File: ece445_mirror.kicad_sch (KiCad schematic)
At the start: 47 parts, among them J1 Conn_01x04, J2 Conn_ARM_SWD_TagConnect_TC2030, J3 Conn_01x06, J4 USB_C_Receptacle_USB2.0_14P, SW1 SW_Push, SW2 SW_Push, U1 STM32F405RGT7, U2 STM32F401RBTx, U3 USBLC6-2SC6, U4 AP2112K-3.3, Y1 25MHz

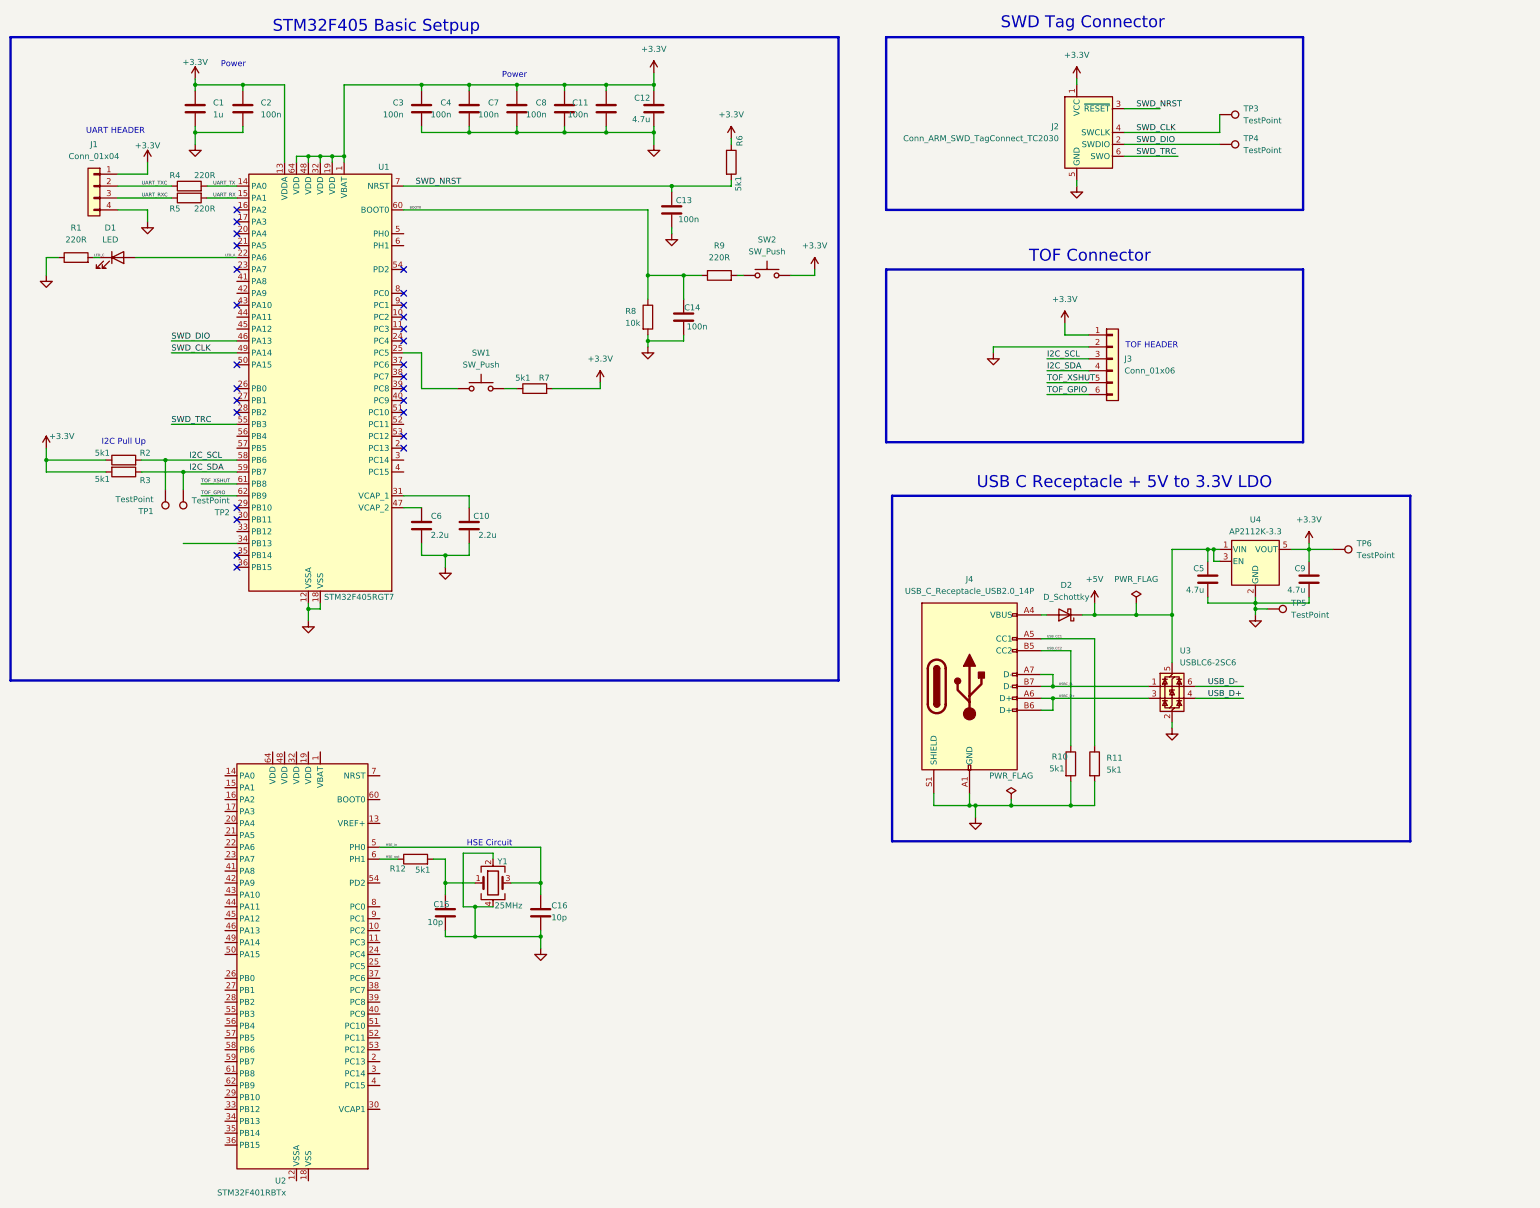
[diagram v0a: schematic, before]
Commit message: schematic completed; changed chip; added HSE, vref+
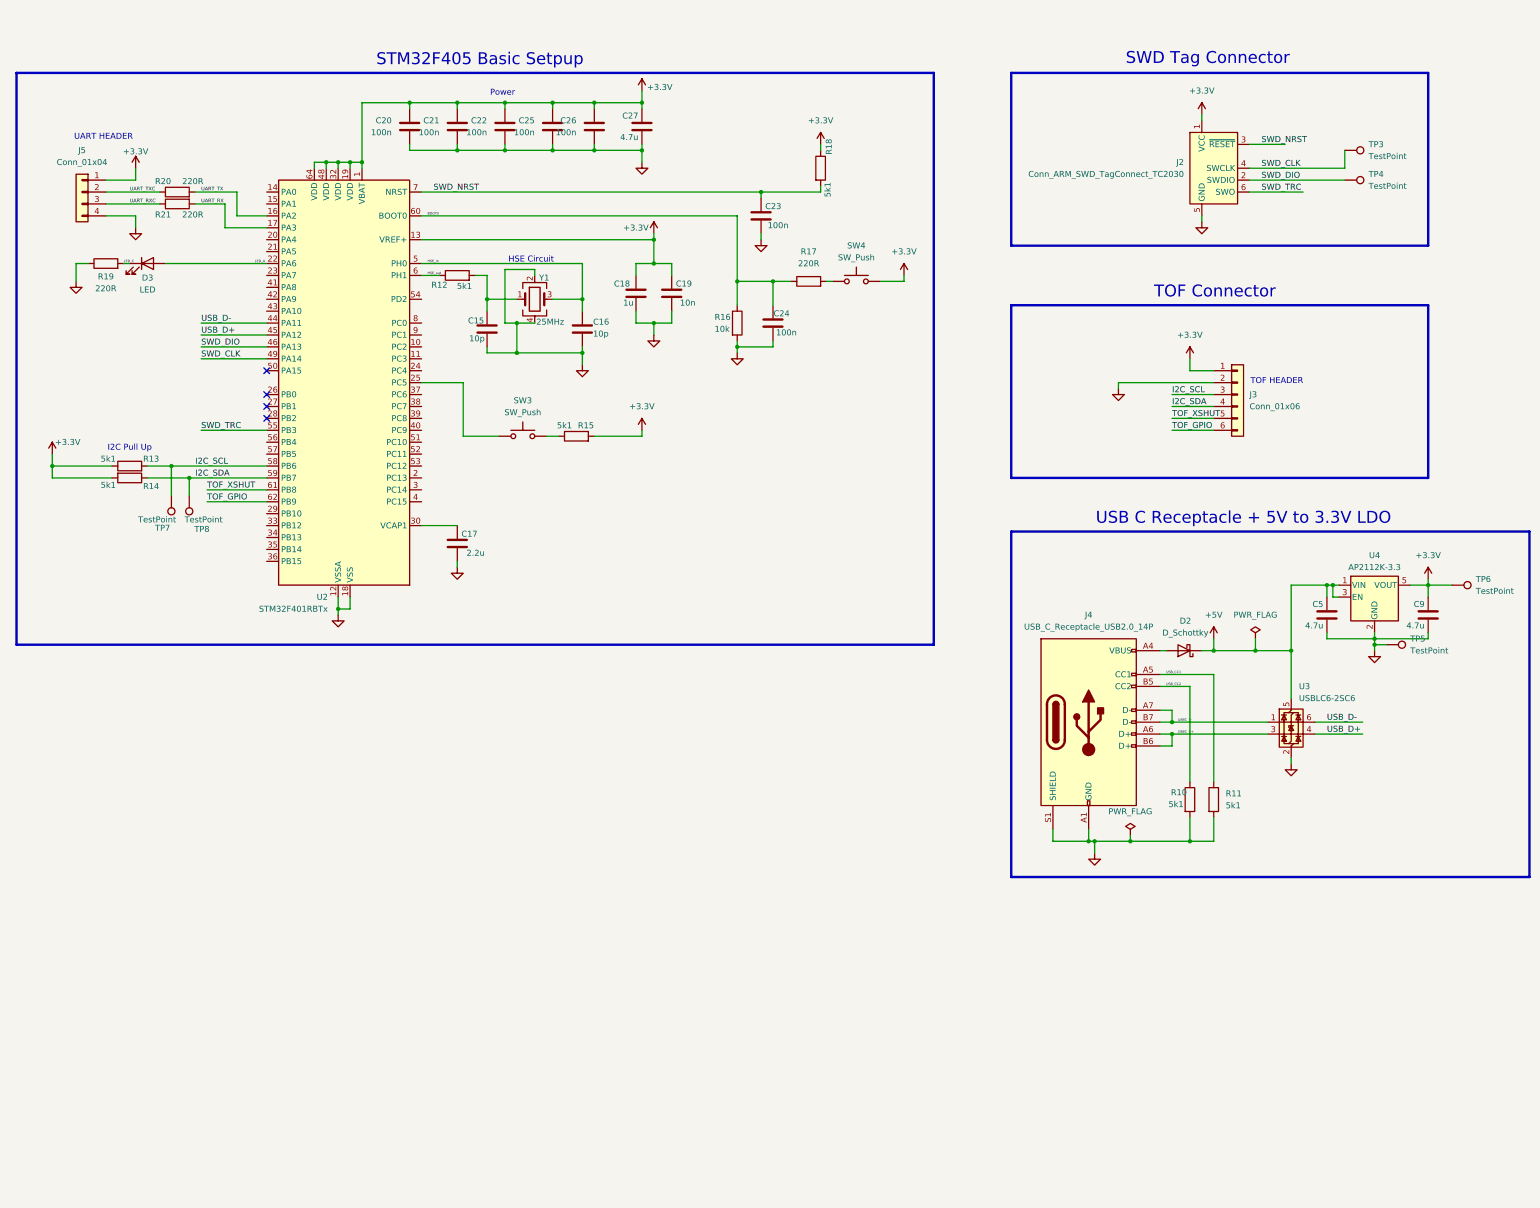
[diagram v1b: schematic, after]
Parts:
- removed C1: 1u, Capacitor_SMD:C_0402_1005Metric, symbol Device:C
- removed C10, C6: 2.2u, Capacitor_SMD:C_0402_1005Metric, symbol Device:C
- removed C11, C13, C14, C2, C3, C4, C7, C8: 100n, Capacitor_SMD:C_0402_1005Metric, symbol Device:C
- removed C12: 4.7u, Capacitor_SMD:C_0805_2012Metric, symbol Device:C
- removed D1: LED, LED_SMD:LED_CSP_Samsung_LH181B_2.36x2.36mm, symbol Device:LED
- removed J1: Conn_01x04, Connector_Molex:Molex_PicoBlade_53261-0471_1x04-1MP_P1.25mm_Horizontal, symbol Connector_Generic:Conn_01x04
- removed R1, R4, R5, R9: 220R, Resistor_SMD:R_0402_1005Metric, symbol Device:R
- removed R2, R3, R6, R7: 5k1, Resistor_SMD:R_0402_1005Metric, symbol Device:R
- removed R8: 10k, Resistor_SMD:R_0402_1005Metric, symbol Device:R
- removed SW1, SW2: SW_Push, Button_Switch_SMD:SW_SPST_CK_RS282G05A3, symbol Switch:SW_Push
- removed TP1, TP2: TestPoint, TestPoint:TestPoint_Pad_2.0x2.0mm, symbol Connector:TestPoint
- removed U1: STM32F405RGT7, Package_QFP:LQFP-64_10x10mm_P0.5mm, symbol MCU_ST_STM32F4:STM32F405RGTx
- added C17: 2.2u, Capacitor_SMD:C_0402_1005Metric, symbol Device:C
- added C18: 1u, Capacitor_SMD:C_0402_1005Metric, symbol Device:C
- added C19: 10n, Capacitor_SMD:C_0402_1005Metric, symbol Device:C
- added C20, C21, C22, C23, C24, C25, C26: 100n, Capacitor_SMD:C_0402_1005Metric, symbol Device:C
- added C27: 4.7u, Capacitor_SMD:C_0805_2012Metric, symbol Device:C
- added D3: LED, LED_SMD:LED_CSP_Samsung_LH181B_2.36x2.36mm, symbol Device:LED
- added J5: Conn_01x04, Connector_Molex:Molex_PicoBlade_53261-0471_1x04-1MP_P1.25mm_Horizontal, symbol Connector_Generic:Conn_01x04
- added R13, R14, R15, R18: 5k1, Resistor_SMD:R_0402_1005Metric, symbol Device:R
- added R16: 10k, Resistor_SMD:R_0402_1005Metric, symbol Device:R
- added R17, R19, R20, R21: 220R, Resistor_SMD:R_0402_1005Metric, symbol Device:R
- added SW3, SW4: SW_Push, Button_Switch_SMD:SW_SPST_CK_RS282G05A3, symbol Switch:SW_Push
- added TP7, TP8: TestPoint, TestPoint:TestPoint_Pad_2.0x2.0mm, symbol Connector:TestPoint
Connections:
- net +3.3V: now also U2.1 (VBAT), U2.13 (VREF+), U2.19 (VDD), U2.32 (VDD), U2.48 (VDD), U2.64 (VDD), C18.1, C19.1, C20.1, C21.1, C22.1, C25.1, C26.1, C27.1, J5.1 (Pin_1), R13.1, R14.2, R15.2, R18.1, SW4.2
- net BOOT0: now also U2.60 (BOOT0), C24.1, R16.1, R17.1
- net GND: now also U2.12 (VSSA), U2.18 (VSS), U2.31 (VSS), U2.47 (VSS), U2.63 (VSS), C17.2, C18.2, C19.2, C20.2, C21.2, C22.2, C23.2, C24.2, C25.2, C26.2, C27.2, J5.4 (Pin_4), R16.2, R19.1
- net I2C_SCL: now also U2.58 (PB6), R13.2, TP7.1
- net I2C_SDA: now also U2.59 (PB7), R14.1, TP8.1
- net LED_A: now also U2.22 (PA6), D3.2 (A)
- net LED_C: now also D3.1 (K), R19.2
- net SWD_CLK: now also U2.49 (PA14)
- net SWD_DIO: now also U2.46 (PA13)
- net SWD_NRST: now also U2.7 (NRST), C23.1, R18.2
- net SWD_TRC: now also U2.55 (PB3)
- net TOF_GPIO: now also U2.62 (PB9)
- net TOF_XSHUT: now also U2.61 (PB8)
- net UART_RX: now also U2.17 (PA3), R21.2
- net UART_RXC: now also J5.3 (Pin_3), R21.1
- net UART_TX: now also U2.16 (PA2), R20.2
- net UART_TXC: now also J5.2 (Pin_2), R20.1
- net USB_D+: now also U2.45 (PA12)
- net USB_D-: now also U2.44 (PA11)
- net at U2.25 (PC5): now also SW3.1
- net at U2.30 (VCAP1): now also C17.1
- new net: R17.2, SW4.1
- new net: R15.1, SW3.2
- no-connect marks 27 -> 4
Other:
- moved on the sheet: C15, C16, C5, C9, D2, J2, J3, J4, R10, R11, R12, TP3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

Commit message: footprints!
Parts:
- removed D3: LED, LED_SMD:LED_CSP_Samsung_LH181B_2.36x2.36mm, symbol Device:LED
- removed J2: Conn_ARM_SWD_TagConnect_TC2030, Connector:Tag-Connect_TC2030-IDC-FP_2x03_P1.27mm_Vertical, symbol Connector:Conn_ARM_SWD_TagConnect_TC2030
- removed R12: 5k1, Resistor_SMD:R_0402_1005Metric, symbol Device:R
- removed R19: 220R, Resistor_SMD:R_0402_1005Metric, symbol Device:R
- removed TP3, TP4: TestPoint, TestPoint:TestPoint_Pad_2.0x2.0mm, symbol Connector:TestPoint
- added J1: Conn_ARM_JTAG_SWD_10, Connector_PinHeader_1.27mm:PinHeader_2x05_P1.27mm_Vertical_SMD, symbol Connector:Conn_ARM_JTAG_SWD_10
- added J2: LED_CONN, Connector_Molex:Molex_KK-254_AE-6410-02A_1x02_P2.54mm_Vertical, symbol Connector_Generic:Conn_01x02
- added R1: 1k, Resistor_SMD:R_0805_2012Metric_Pad1.20x1.40mm_HandSolder, symbol Device:R
- added TP1, TP2: TestPoint, TestPoint:TestPoint_Pad_2.0x2.0mm, symbol Connector:TestPoint
- C15, C16: footprint Capacitor_SMD:C_0201_0603Metric -> Capacitor_SMD:C_0805_2012Metric_Pad1.18x1.45mm_HandSolder
- C17: footprint Capacitor_SMD:C_0402_1005Metric -> Capacitor_SMD:C_1206_3216Metric_Pad1.33x1.80mm_HandSolder
- C18, C19: footprint Capacitor_SMD:C_0402_1005Metric -> Capacitor_SMD:C_0805_2012Metric_Pad1.18x1.45mm_HandSolder
- C20, C21, C22, C23, C24, C25, C26: footprint Capacitor_SMD:C_0402_1005Metric -> Capacitor_SMD:C_0603_1608Metric_Pad1.08x0.95mm_HandSolder
- C27, C5, C9: footprint Capacitor_SMD:C_0805_2012Metric -> Capacitor_SMD:C_1206_3216Metric_Pad1.33x1.80mm_HandSolder
- D2: footprint Diode_SMD:D_2114_3652Metric_Pad1.85x3.75mm_HandSolder -> Diode_THT:D_DO-41_SOD81_P10.16mm_Horizontal
- J3: footprint (none) -> Connector_Molex:Molex_KK-254_AE-6410-06A_1x06_P2.54mm_Vertical
- J5: footprint Connector_Molex:Molex_PicoBlade_53261-0471_1x04-1MP_P1.25mm_Horizontal -> Connector_Molex:Molex_KK-254_AE-6410-04A_1x04_P2.54mm_Vertical
- R10, R11, R13, R14, R15, R16, R18: footprint Resistor_SMD:R_0402_1005Metric -> Resistor_SMD:R_0805_2012Metric_Pad1.20x1.40mm_HandSolder
- R17, R20, R21: footprint Resistor_SMD:R_0402_1005Metric -> Resistor_SMD:R_0603_1608Metric_Pad0.98x0.95mm_HandSolder
- Y1: footprint DroneSensorAndControl_PCBFootprints:CRYSTAL_ABM8G_ABR(HSE) -> ece445_PCBFootprints:OSCCC200X160X50N
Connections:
- net +3.3V: now also J1.1 (VTref)
- net GND: now also J1.3 (GND), J1.5 (GND), J1.9 (GNDDetect), J2.1 (Pin_1)
- net HSE_out: now also C15.1, Y1.1
- net LED_A: now also R1.2
- net SWD_CLK: now also J1.4 (SWCLK/TCK), TP1.1
- net SWD_DIO: now also J1.2 (SWDIO/TMS), TP2.1
- net SWD_NRST: now also J1.10 (~{RESET})
- net SWD_TRC: now also J1.6 (SWO/TDO)
- new net: J2.2 (Pin_2), R1.1
- no-connect marks 4 -> 5
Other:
- note added: "SWD Header"
- note removed: "SWD Tag Connector"
- moved on the sheet: C5, C9, D2, J3, J4, R10, R11, TP5, TP6, U3, U4

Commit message: placement done
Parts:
- removed SW3, SW4: SW_Push, Button_Switch_SMD:SW_SPST_CK_RS282G05A3, symbol Switch:SW_Push
- added C1: 1u, Capacitor_SMD:C_0805_2012Metric_Pad1.18x1.45mm_HandSolder, symbol Device:C
- added J6: button, Connector_Molex:Molex_KK-254_AE-6410-02A_1x02_P2.54mm_Vertical, symbol Connector_Generic:Conn_01x02
- added J7: boot_switch, Connector_Molex:Molex_KK-254_AE-6410-02A_1x02_P2.54mm_Vertical, symbol Connector_Generic:Conn_01x02
- added J8: Photoresistor, Connector_Molex:Molex_KK-254_AE-6410-02A_1x02_P2.54mm_Vertical, symbol Connector_Generic:Conn_01x02
- added J9: LED_STRIP, Connector_Molex:Molex_KK-254_AE-6410-02A_1x02_P2.54mm_Vertical, symbol Connector_Generic:Conn_01x02
- added R2: 1k, Resistor_SMD:R_0805_2012Metric_Pad1.20x1.40mm_HandSolder, symbol Device:R
- added R3: 220R, Resistor_SMD:R_0603_1608Metric_Pad0.98x0.95mm_HandSolder, symbol Device:R
- D2: footprint Diode_THT:D_DO-41_SOD81_P10.16mm_Horizontal -> Diode_SMD:D_0603_1608Metric_Pad1.05x0.95mm_HandSolder
- R15: value 5k1 -> 10k
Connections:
- net +3.3V: now also J6.1 (Pin_1), J7.1 (Pin_1), R2.2; no longer R15.2
- net +5V: now also J9.2 (Pin_2), R3.1
- net GND: now also C1.2, J8.1 (Pin_1), J9.1 (Pin_1)
- net at R17.2: now also J7.2 (Pin_2)
- net at R15.1: now also U2.25 (PC5), C1.1
- net at U2.23 (PA7): now also J8.2 (Pin_2), R2.1
- net LED_STRIP: now reaches U2.42 (PA9)
- net LED_STRIP: now also R3.2
- new net: J6.2 (Pin_2), R15.2
- no-connect marks 5 -> 34
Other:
- note added: "LED STRIP"
- note added: "STM32F401 Basic Setpup"
- note removed: "STM32F405 Basic Setpup"
- moved on the sheet: J2, R1, R15
